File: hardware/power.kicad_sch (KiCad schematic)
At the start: 35 parts, among them J1 Battery, U1 BQ24073RGTR, U2 TPS63001DRCR, U3 LP5907MFX-1.8, U4 LP5907MFX-1.8, U5 LP5907MFX-1.8, U6 TPS61023DRLR, U7 TPS2553DBVR

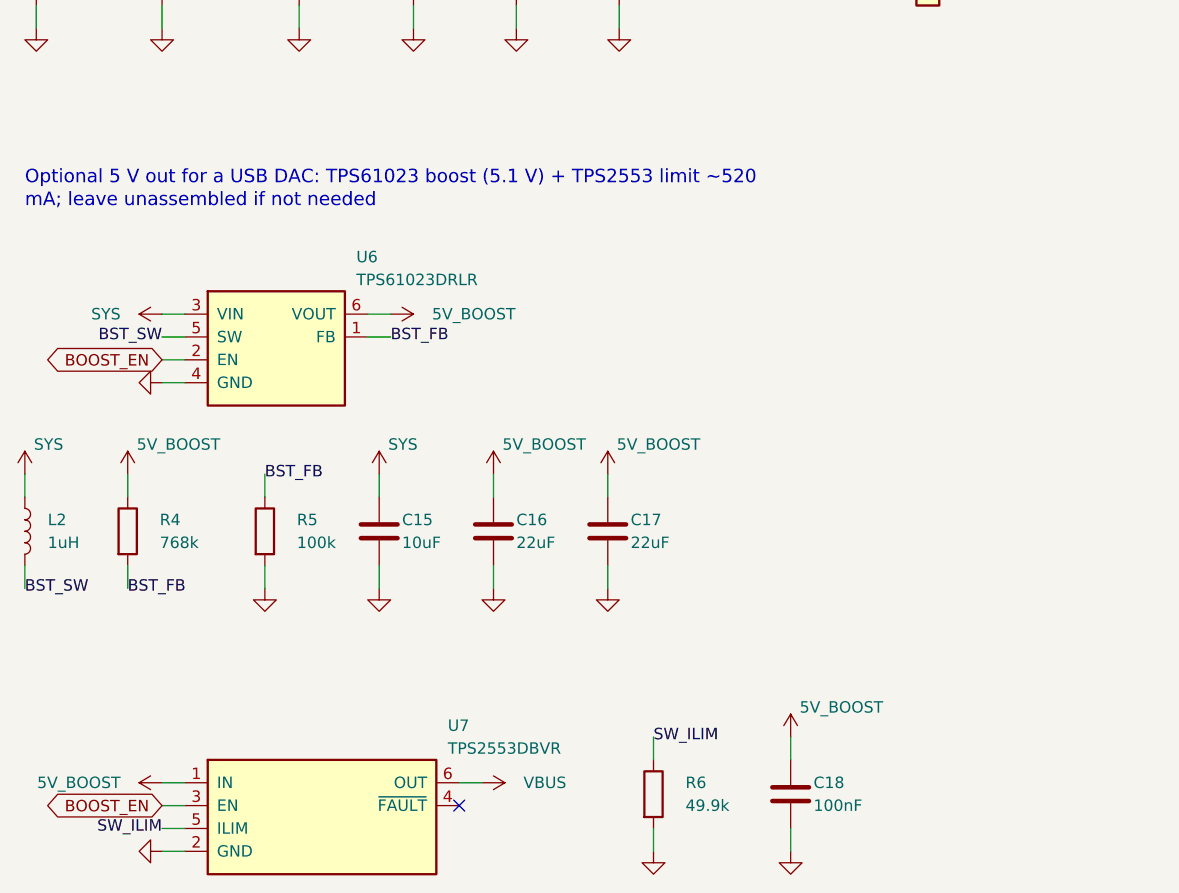
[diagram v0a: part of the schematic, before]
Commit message: Use the chosen parts in the schematic, with their LCSC numbers
The headphone jacks are now real parts. The 3.5 mm SHOU HAN PJ-342 is a
3-pole stereo jack, per its drawing: tip 3, ring 6, sleeve 5 and 2, and a
switch on tip and ring that touches them while no plug is in. Its tip
switch drives the left DAC's HP_DETECT, so the firmware sets
HPDETECT_INV. The 4.4 mm jack is the Kinghelm KH-PJ-44002-12DBAP-A: two
pins per pole in Pentaconn order and a separate plug switch from DET_44
to ground.

Checked against the datasheets: the oscillators' OE is high or open =
running and tri-state when low, so they can share MCLK; the GL823K's VDD
and VDDA are both its own 3.3 V. The CS43131 FILT capacitors are 22 uF
0805 25 V now, about 15-19 uF under bias where a 15 uF part would keep
about 11. The e-paper circuit follows the GDEY037T03-T02 reference: VPP
(pin 19) left open and a 1 MOhm gate pull-down, R1 and R2 in 0603.

Every assembled part has an LCSC number: the passives are in a table
checked on lcsc.com. 49.9k had no stock, so the TPS2553 limit resistor is
47k (about 0.5 A). The touch and microSD footprints are the real ones.
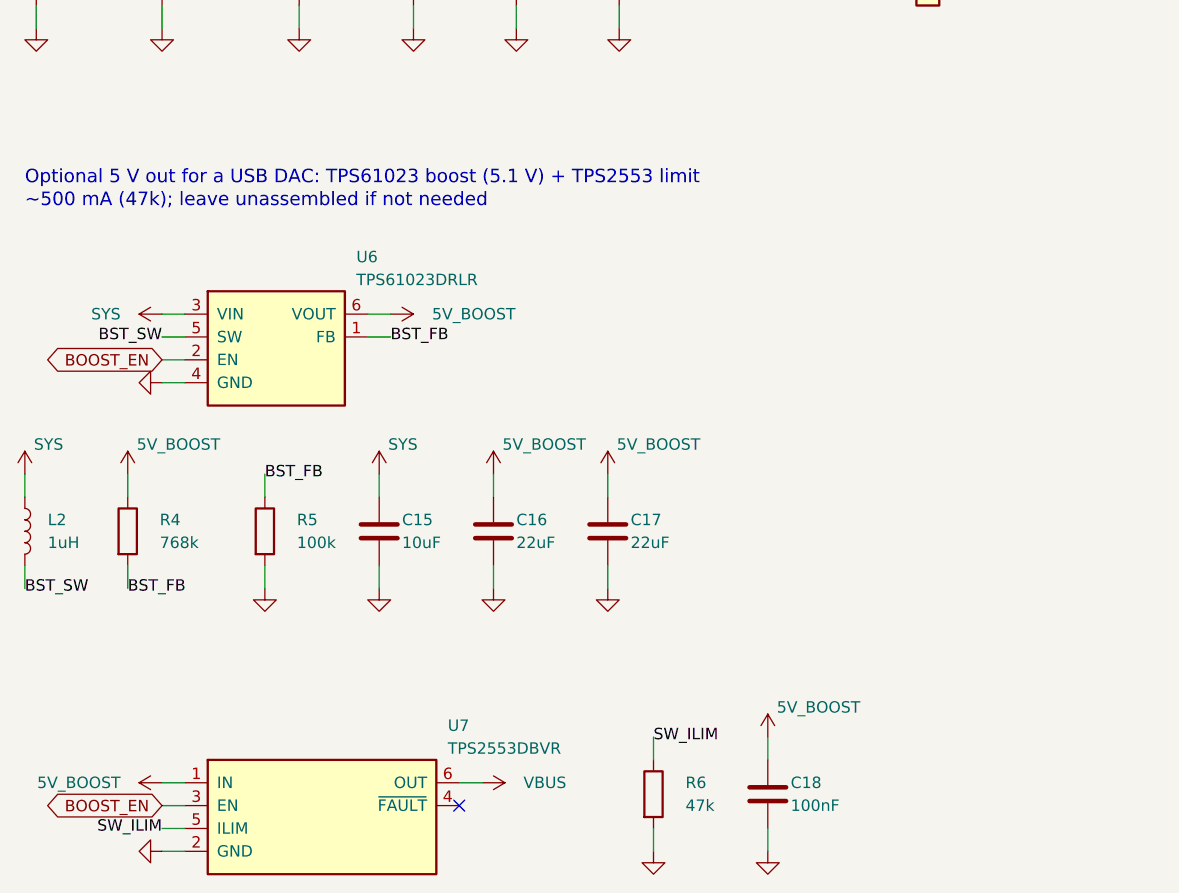
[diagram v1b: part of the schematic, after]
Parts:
- C1: LCSC (none) -> C15849
- C10, C11, C12, C13, C8, C9: LCSC (none) -> C52923
- C14, C15, C2, C3, C4: LCSC (none) -> C15850
- C16, C17, C6, C7: LCSC (none) -> C45783
- C18, C5: LCSC (none) -> C1525
- FB1: LCSC (none) -> C85833
- L1: LCSC (none) -> C5291780
- L2: LCSC (none) -> C354542
- R1: LCSC (none) -> C25860
- R2: LCSC (none) -> C61897
- R3: LCSC (none) -> C36871
- R4: LCSC (none) -> C27017
- R5: LCSC (none) -> C25741
- R6: value 49.9k -> 47k; LCSC (none) -> C25792
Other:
- note added: "Optional 5 V out for a USB DAC: TPS61023 boost (5.1 V) + TPS2553 limit"
- note added: "~500 mA (47k); leave unassembled if not needed"
- note removed: "Optional 5 V out for a USB DAC: TPS61023 boost (5.1 V) + TPS2553 limit ~520"
- note removed: "mA; leave unassembled if not needed"
